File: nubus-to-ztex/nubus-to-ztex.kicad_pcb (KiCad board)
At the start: 4 copper layers, 161.6 x 100 mm, 125 parts, among them J1 Conn_02x07_Odd_Even, J2 Conn_02x07_Odd_Even, J3 Conn_01x06_Male, J4 C96ABC, J5 HDMI_A, J6 USB micro-B, J7 Conn_01x03_Male, J8 Conn_01x02, J9 DB15_Female_HighDensity_Mount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, U1 74LVT125, U10 SN65220, U11 TPS2051C, U12 ADV7125-lqfp48, U13 AD1580, U2 74LVT125, U3 74LVT125, U4 XC9572XL-VQ64, U5 74LVT245BPW,118, U6 74LVT245BPW,118, U7 74LVT245BPW,118, U8 74LVT245BPW,118, U9 TPD12S016PWR

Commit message: drop vga
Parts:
- removed C30, C31, C32, C33: 100nF, Capacitor_SMD:C_0603_1608Metric
- removed C34, C35, C36: 10nF, Capacitor_SMD:C_0603_1608Metric
- removed C37, C38: 1uF, Capacitor_SMD:C_0603_1608Metric
- removed J9: DB15_Female_HighDensity_MountingHoles, For_SeeedStudio:L77HDE15SD1CH4RHNVGA
- removed R28: 536, Resistor_SMD:R_0603_1608Metric
- removed R29: 1k, Resistor_SMD:R_0603_1608Metric
- removed R30, R31, R32: 75, Resistor_SMD:R_0603_1608Metric
- removed R34, R35: 100, Resistor_SMD:R_0603_1608Metric
- removed U12: ADV7125-lqfp48, For_SeeedStudio:ADV7125KSTZ140
- removed U13: AD1580, Package_TO_SOT_SMD:SOT-23
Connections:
- JCD1 pad 20: FPGA_VGA_HS -> Net-(JCD1-Pad20)
- JCD1 pad 22: FPGA_VGA_VS -> Net-(JCD1-Pad22)
- JCD1 pad 29: FPGA_VGA_CLK -> Net-(JCD1-Pad29)
- JCD1 pad 37: FPGA_B7 -> Net-(JCD1-Pad37)
- JCD1 pad 38: FPGA_R0 -> Net-(JCD1-Pad38)
- JCD1 pad 39: FPGA_B6 -> Net-(JCD1-Pad39)
- JCD1 pad 40: FPGA_R1 -> Net-(JCD1-Pad40)
- JCD1 pad 41: FPGA_B5 -> Net-(JCD1-Pad41)
- JCD1 pad 42: FPGA_R2 -> Net-(JCD1-Pad42)
- JCD1 pad 43: FPGA_B4 -> Net-(JCD1-Pad43)
- JCD1 pad 44: FPGA_R3 -> Net-(JCD1-Pad44)
- JCD1 pad 45: FPGA_B3 -> Net-(JCD1-Pad45)
- JCD1 pad 46: FPGA_R4 -> Net-(JCD1-Pad46)
- JCD1 pad 47: FPGA_B2 -> Net-(JCD1-Pad47)
- JCD1 pad 48: FPGA_R5 -> Net-(JCD1-Pad48)
- JCD1 pad 49: FPGA_B1 -> Net-(JCD1-Pad49)
- JCD1 pad 50: FPGA_R6 -> Net-(JCD1-Pad50)
- JCD1 pad 51: FPGA_B0 -> Net-(JCD1-Pad51)
- JCD1 pad 52: FPGA_R7 -> Net-(JCD1-Pad52)
- JCD1 pad 53: FPGA_G7 -> Net-(JCD1-Pad53)
- JCD1 pad 54: FPGA_G0 -> Net-(JCD1-Pad54)
- JCD1 pad 55: FPGA_G6 -> Net-(JCD1-Pad55)
- JCD1 pad 56: FPGA_G1 -> Net-(JCD1-Pad56)
- JCD1 pad 57: FPGA_G5 -> Net-(JCD1-Pad57)
- JCD1 pad 58: FPGA_G2 -> Net-(JCD1-Pad58)
- JCD1 pad 59: FPGA_G4 -> Net-(JCD1-Pad59)
- JCD1 pad 60: FPGA_G3 -> Net-(JCD1-Pad60)
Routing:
- net GND: track 1359.9 -> 1095.4 mm, vias 65 -> 52
- net FPGA_VGA_HS: track 105.2 -> 0.00 mm, vias 1 -> 0
- net FPGA_VGA_VS: track 103.2 -> 0.00 mm, vias 1 -> 0
- net FPGA_R1: track 90.2 -> 0.00 mm
- net FPGA_B2: track 90.1 -> 0.00 mm
- net FPGA_G7: track 90.0 -> 0.00 mm
- net FPGA_R4: track 90.0 -> 0.00 mm
- net FPGA_B4: track 90.0 -> 0.00 mm
- net FPGA_G4: track 90.0 -> 0.00 mm
- net FPGA_R5: track 90.0 -> 0.00 mm
- net FPGA_R3: track 90.0 -> 0.00 mm
- net FPGA_B3: track 90.0 -> 0.00 mm
- net FPGA_G6: track 90.0 -> 0.00 mm
- net FPGA_G0: track 90.0 -> 0.00 mm
- net FPGA_G5: track 90.0 -> 0.00 mm
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
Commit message: forgot to commit last attempt at V1.2
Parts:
- removed C13: 1uF, Capacitor_SMD:C_0603_1608Metric
- removed C15: 10nF, Capacitor_SMD:C_0603_1608Metric
- removed C16: 100nF, Capacitor_SMD:C_0603_1608Metric
- removed D10, D15, D16, D6, D7, D8, D9: YELLOW, LED_SMD:LED_0805_2012Metric
- removed R11, R12, R13, R14, R15, R20, R21: 549, Resistor_SMD:R_0603_1608Metric
- added C30: 100nF, Capacitor_SMD:C_0603_1608Metric, F.Cu at (137.7, 46.8)
- added J9: Conn_02x06_Odd_Even, For_SeeedStudio:PinSocket_2x06_P2.54mm_Horizontal_For_SeeedStudio, F.Cu at (124.3, 49.9)
- added U12: 74CB3T1G125DBVR, Package_TO_SOT_SMD:SOT-23-5, F.Cu at (149.9, 48.5)
- added U13: SN74CB3T3125PWR, Package_SO:TSSOP-14_4.4x5mm_P0.65mm, F.Cu at (186.6, 50.8)
- added U14: SN74CB3T3245PWR, For_SeeedStudio:TSSOP-20_4.4x6.5mm_P0.65mm_ForSeeedStudio, F.Cu at (142.2, 48.8)
- C10: value 100nF -> 47uF; footprint Capacitor_SMD:C_0603_1608Metric -> Capacitor_SMD:C_0805_2012Metric
- C11, C7, C8: value 10nF -> 100nF
- D4, D5: value ORANGE -> RED
- J2: value Conn_02x07_Odd_Even -> 47219-2001; footprint For_SeeedStudio:PinHeader_2x07_P2.00mm_Vertical_For_SeeedStudio -> MOLEX_47219-2001:MOLEX_47219-2001
- U4: value XC9572XL-VQ64 -> SN74CB3T3125PWR; footprint For_SeeedStudio:TQFP-64_10x10mm_P0.5mm_Xlinx -> Package_SO:TSSOP-14_4.4x5mm_P0.65mm
- moved J2 74.9 mm to (156.8, 12.6), turned to 0 degrees
- moved C9 59.7 mm to (157.0, 21.4), turned to 0 degrees
- moved C8 56.2 mm to (190.2, 47.0), turned to 180 degrees
- moved C10 56.1 mm to (157.0, 23.6), turned to 0 degrees
- moved D2 43.9 mm to (189.4, 16.0)
- moved R2 43.9 mm to (189.4, 19.6)
- moved D1 43.9 mm to (187.1, 16.0)
- moved R1 43.9 mm to (187.1, 19.6)
- moved D5 38.8 mm to (193.9, 16.0), turned to 270 degrees
- moved D4 36.2 mm to (191.6, 16.0), turned to 270 degrees
- moved R10 34.5 mm to (193.9, 19.6), turned to 90 degrees
- moved C39 32.8 mm to (265.8, 43.4), turned to 180 degrees
- moved R9 32.1 mm to (191.6, 19.6), turned to 90 degrees
- moved R33 28.9 mm to (264.4, 37.6), turned to 180 degrees
- moved C11 28.4 mm to (147.0, 49.4), turned to 270 degrees
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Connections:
- D4 pad 1: ARB -> GND
- D5 pad 1: GRANT -> GND
- J2 pad 1: GND -> SD_D2
- J2 pad 2: +3V3 -> SD_D3
- J2 pad 3: GND -> SD_CMD
- J2 pad 4: CPLD_JTAG_TMS -> +3V3
- J2 pad 5: GND -> SD_CLK
- J2 pad 6: CPLD_JTAG_TCK -> GND
- J2 pad 7: GND -> SD_D0
- J2 pad 8: CPLD_JTAG_TDO -> SD_D1
- JAB1 pad 10: ~ACK_3V3 -> RQST_o_n
- JAB1 pad 11: GRANT -> START_o_n
- JAB1 pad 12: ARB -> ACK_oe_n
- JAB1 pad 13: fpga_to_cpld_signal -> ARB0_o_n
- JAB1 pad 14: fpga_to_cpld_clk -> ACK_o_n
- JAB1 pad 15: NUBUS_MASTER_DIR -> ARB3_o_n
- JAB1 pad 16: fpga_to_cpld_signal_2 -> ARB2_o_n
- JAB1 pad 17: ~RESET_3V3 -> NUBUS_AD_DIR
- JAB1 pad 18: NUBUS_AD_DIR -> ARB1_o_n
- JAB1 pad 7: ~TM0_3V3 -> ~START_3V3
- JAB1 pad 8: ~TM1_3V3 -> ~ACK_3V3
- JAB1 pad 9: ~START_3V3 -> START_oe_n
- JCD1 pad 11: tmoen -> ~ARB3_3V3
- JCD1 pad 12: LED0 -> ~ARB2_3V3
- JCD1 pad 13: HDMI_HPD_A -> ~ARB0_3V3
- JCD1 pad 14: LED1 -> ~ARB1_3V3
- JCD1 pad 15: HDMI_SDA_A -> PMOD-6
- JCD1 pad 17: HDMI_SCL_A -> PMOD-5
- JCD1 pad 18: ~TM2_3V3 -> SD_D1
- JCD1 pad 19: HDMI_CEC_A -> PMOD-8
- JCD1 pad 20: Net-(JCD1-Pad20) -> SD_D0
- JCD1 pad 21: HDMI_CLK+ -> PMOD-7
- JCD1 pad 22: Net-(JCD1-Pad22) -> SD_CLK
- JCD1 pad 23: HDMI_CLK- -> PMOD-10
- JCD1 pad 24: HDMI_D0- -> SD_CMD
- JCD1 pad 25: HDMI_D1- -> PMOD-9
- JCD1 pad 26: HDMI_D0+ -> SD_D3
- JCD1 pad 27: HDMI_D1+ -> PMOD-12
- JCD1 pad 28: HDMI_D2- -> SD_D2
- JCD1 pad 29: Net-(JCD1-Pad29) -> PMOD-11
- JCD1 pad 30: HDMI_D2+ -> TMx_oe_n
- JCD1 pad 37: Net-(JCD1-Pad37) -> HDMI_HPD_A
- JCD1 pad 38: Net-(JCD1-Pad38) -> ~TM0_3V3
- JCD1 pad 39: Net-(JCD1-Pad39) -> HDMI_SDA_A
- JCD1 pad 40: Net-(JCD1-Pad40) -> ~TM1_3V3
- JCD1 pad 41: Net-(JCD1-Pad41) -> HDMI_SCL_A
- JCD1 pad 42: Net-(JCD1-Pad42) -> TM1_n_o
- JCD1 pad 43: Net-(JCD1-Pad43) -> HDMI_CEC_A
- JCD1 pad 44: Net-(JCD1-Pad44) -> TM0_n_o
- JCD1 pad 45: Net-(JCD1-Pad45) -> HDMI_CLK-
- JCD1 pad 46: Net-(JCD1-Pad46) -> TM2_oe_n
- JCD1 pad 47: Net-(JCD1-Pad47) -> HDMI_CLK+
- JCD1 pad 48: Net-(JCD1-Pad48) -> TM2_o_n
- JCD1 pad 49: Net-(JCD1-Pad49) -> HDMI_D0+
- JCD1 pad 50: Net-(JCD1-Pad50) -> ~TM2_3V3
- JCD1 pad 51: Net-(JCD1-Pad51) -> HDMI_D0-
- JCD1 pad 52: Net-(JCD1-Pad52) -> ~RESET_3V3
- JCD1 pad 53: Net-(JCD1-Pad53) -> HDMI_D1+
- JCD1 pad 54: Net-(JCD1-Pad54) -> LED0
- JCD1 pad 55: Net-(JCD1-Pad55) -> HDMI_D1-
- JCD1 pad 56: Net-(JCD1-Pad56) -> LED1
- JCD1 pad 57: Net-(JCD1-Pad57) -> HDMI_D2-
- JCD1 pad 58: Net-(JCD1-Pad58) -> LED2
- JCD1 pad 59: Net-(JCD1-Pad59) -> HDMI_D2+
- JCD1 pad 60: Net-(JCD1-Pad60) -> LED3
- R10 pad 1: +3V3 -> LED3
- R9 pad 1: +3V3 -> LED2
- U4 pad 1: ~ID3_3V3 -> GND
- U4 pad 10: ~ACK_5V -> GND
- U4 pad 11: START_oe_n -> ~START_5V
- U4 pad 12: START_o_n -> ~START_3V3
- U4 pad 13: ~START_5V -> GND
- U4 pad 14: GND -> +3V3
- U4 pad 2: ~ACK_3V3 -> ~RQST_3V3
- U4 pad 3: +3V3 -> ~RQST_5V
- U4 pad 4: ~START_3V3 -> GND
- U4 pad 5: RQST_o_n -> ~ACK_3V3
- U4 pad 6: ~RQST_5V -> ~ACK_5V
- U4 pad 7: ~ID3_5V -> GND
- U4 pad 8: ACK_oe_n -> ~CLK_5V
- U4 pad 9: ACK_o_n -> ~CLK_3V3
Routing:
- net GND: track 1095.4 -> 1284.8 mm, vias 52 -> 63
- net +3V3: track 671.1 -> 737.6 mm, vias 30 -> 27
- net ARB: track 60.1 -> 0.00 mm, vias 1 -> 0
- net GRANT: track 57.0 -> 0.00 mm, vias 1 -> 0
- net PMOD-11: track 0.00 -> 54.7 mm
- net PMOD-12: track 0.00 -> 54.7 mm
- net HDMI_D2+: track 138.3 -> 83.7 mm
- net HDMI_D2-: track 137.6 -> 85.3 mm
- net HDMI_D1+: track 139.8 -> 88.0 mm
- net HDMI_D1-: track 138.8 -> 87.1 mm
- net PMOD-10: track 0.00 -> 48.6 mm
- net PMOD-9: track 0.00 -> 48.6 mm
- net tmoen: track 43.2 -> 0.00 mm
- net PMOD-8: track 0.00 -> 42.5 mm
- net PMOD-7: track 0.00 -> 42.5 mm
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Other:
- board text added: "NuBusFPGA V1.2"
- board text added: "PMOD"
- board text added: "User LED 0..3"
- board text added: "micro-sd"
- board text removed: "ACK"
- board text removed: "AD0/1"
- board text removed: "ARB GRANT"
- board text removed: "CPLD JTAG"
- board text removed: "NuBusFPGA V1.0"
- board text removed: "Reset"
- board text removed: "TM0/1"
- board text removed: "User LED 0..1"
- board text removed: "VGA ctrl"

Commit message: more stuff thinking about V1.2
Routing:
- net ~ID0_5V: track 49.7 -> 48.6 mm
- net ~ID1_5V: track 55.7 -> 54.7 mm
- net ~ID3_5V: track 58.6 -> 57.7 mm
- net ~ID2_5V: track 52.1 -> 51.3 mm
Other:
- board text removed: "VGA"

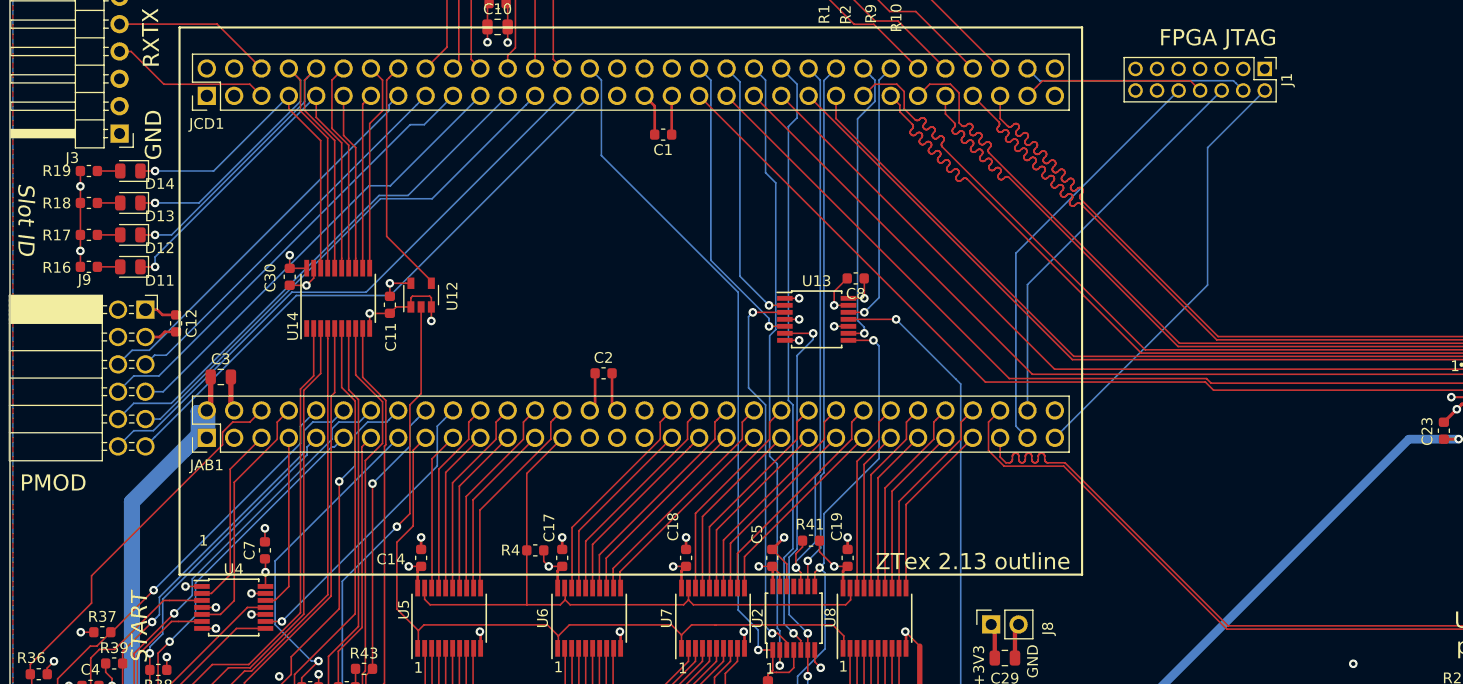
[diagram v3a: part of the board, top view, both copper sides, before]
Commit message: cleanups, alternative MPN for 2x32 headers (TBC)
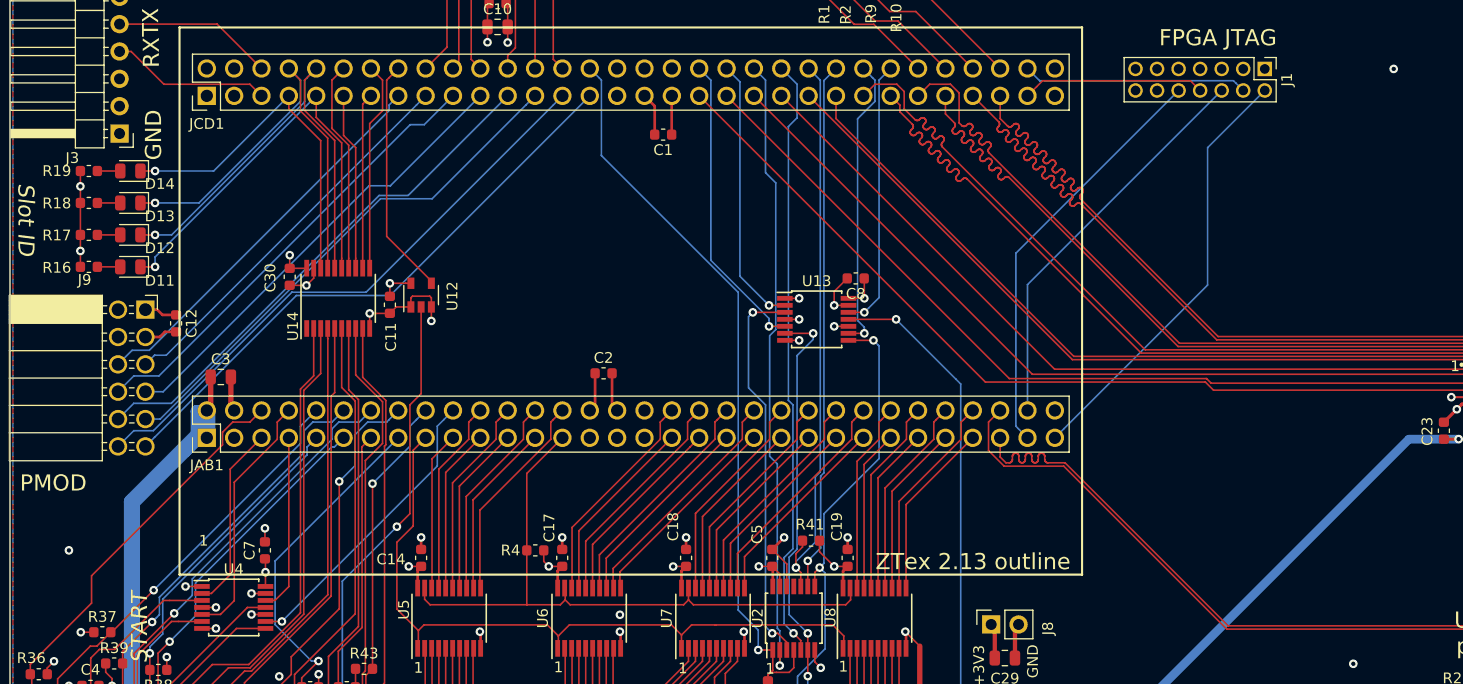
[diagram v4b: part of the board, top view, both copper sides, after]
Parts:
- U12: value 74CB3T1G125DBVR -> SN74CB3T1G125DBVR
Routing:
- net GND: vias 63 -> 66
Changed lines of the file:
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@@
     (thickness 1.6)
     (drawings 114)
-    (tracks 3059)
+    (tracks 3065)
     (zones 0)
     (modules 94)
@@
       (effects (font (size 1 1) (thickness 0.15)))
     )
-    (fp_text value 74CB3T1G125DBVR (at 0 2.9 90) (layer F.Fab)
+    (fp_text value SN74CB3T1G125DBVR (at 0 2.9 90) (layer F.Fab)
       (effects (font (size 1 1) (thickness 0.15)))
     )
@@
   (segment (start 123.8 97.46) (end 124.896015 97.46) (width 1.5) (layer In1.Cu) (net 1) (status 10))
   (segment (start 257.03 39.71) (end 256.97 39.77) (width 0.1524) (layer In1.Cu) (net 1))
-  (segment (start 168.3575 74.27) (end 168.3575 79.75) (width 0.1524) (layer In1.Cu) (net 1))
+  (segment (start 168.3575 74.27) (end 168.3575 78.18) (width 0.1524) (layer In1.Cu) (net 1))
   (segment (start 145.3 88.2) (end 145.4 88.1) (width 0.1524) (layer In1.Cu) (net 1))
   (via (at 263.2 67.3575) (size 0.8) (drill 0.4) (layers F.Cu B.Cu) (net 1))
@@
   (segment (start 205.0375 82.2) (end 205.0375 79.4125) (width 0.4) (layer F.Cu) (net 1) (status 30))
   (segment (start 208.74 30) (end 208.74 27.46) (width 1.5) (layer In1.Cu) (net 1) (status 30))
-  (segment (start 240.2 27.5) (end 242.87 30.17) (width 0.1524) (layer In1.Cu) (net 1))
+  (segment (start 240.2 27.5) (end 240.2 27.5) (width 0.1524) (layer In1.Cu) (net 1))
   (segment (start 228.23 27.5) (end 240.2 27.5) (width 0.8) (layer In1.Cu) (net 1) (status 10))
   (segment (start 115.2 90.73) (end 115.2 95.42533) (width 0.1524) (layer In1.Cu) (net 1))
@@
   (segment (start 185 48.8) (end 179.08 48.8) (width 0.1524) (layer In1.Cu) (net 1))
   (segment (start 123.5 65.9) (end 127.5 65.9) (width 0.1524) (layer In1.Cu) (net 1))
-  (segment (start 117.2 72.2) (end 123.5 65.9) (width 0.1524) (layer In1.Cu) (net 1))
+  (segment (start 117.2 72.2) (end 117.2 72.2) (width 0.1524) (layer In1.Cu) (net 1))
   (segment (start 117.2 84.78) (end 117.2 72.2) (width 0.1524) (layer In1.Cu) (net 1))
   (segment (start 149.925 17.3) (end 149.925 16.1226) (width 0.1524) (layer F.Cu) (net 1))
@@
   (via (at 118.53467 98.72) (size 0.8) (drill 0.4) (layers F.Cu B.Cu) (net 1))
   (segment (start 158.1 97.46) (end 158.1 102.8) (width 0.5) (layer In1.Cu) (net 1))
+  (segment (start 240.2 27.5) (end 242.87 30.17) (width 0.1524) (layer In1.Cu) (net 1))
+  (via (at 240.2 27.5) (size 0.8) (drill 0.4) (layers F.Cu B.Cu) (net 1))
+  (segment (start 117.2 72.2) (end 123.5 65.9) (width 0.1524) (layer In1.Cu) (net 1))
+  (via (at 117.2 72.2) (size 0.8) (drill 0.4) (layers F.Cu B.Cu) (net 1))
+  (segment (start 168.3575 78.18) (end 168.3575 79.75) (width 0.1524) (layer In1.Cu) (net 1))
+  (via (at 168.3575 78.18) (size 0.8) (drill 0.4) (layers F.Cu B.Cu) (net 1))
   (segment (start 209.589999 60.900001) (end 208.74 61.75) (width 0.1524) (layer B.Cu) (net 2) (status 30))
   (segment (start 222.921399 34.808601) (end 222.921399 47.568601) (width 0.1524) (layer B.Cu) (net 2))
@@
     (connect_pads (clearance 0.508))
     (min_thickness 0.254)
-    (fill (arc_segments 16) (thermal_gap 0.508) (thermal_bridge_width 0.508))
+    (fill yes (arc_segments 16) (thermal_gap 0.508) (thermal_bridge_width 0.508))
     (polygon
       (pts
@@
     (connect_pads (clearance 0.508))
     (min_thickness 0.254)
-    (fill (arc_segments 16) (thermal_gap 0.508) (thermal_bridge_width 0.508))
+    (fill yes (arc_segments 16) (thermal_gap 0.508) (thermal_bridge_width 0.508))
     (polygon
       (pts
@@
     (connect_pads (clearance 0.508))
     (min_thickness 0.254)
-    (fill (arc_segments 16) (thermal_gap 0.508) (thermal_bridge_width 0.508))
+    (fill yes (arc_segments 16) (thermal_gap 0.508) (thermal_bridge_width 0.508))
     (polygon
       (pts
@@
     (connect_pads (clearance 0.508))
     (min_thickness 0.254)
-    (fill (arc_segments 16) (thermal_gap 0.508) (thermal_bridge_width 0.508))
+    (fill yes (arc_segments 16) (thermal_gap 0.508) (thermal_bridge_width 0.508))
     (polygon
       (pts
